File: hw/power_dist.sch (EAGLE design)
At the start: 72 parts, among them J1 JST-ZH6SMT_VERT, J2 JST-PH4SMT_VERT, J3 JST-PH5VERT, P1 XT30P, P2 XT30P, P3 XT30P, P4 XT30P, P5 XT30P, P6 XT30P, P7 XT90PW-M, Q1 PSMN4R8-100BSEJ, Q2 PSMN4R8-100BSEJ, Q3 PSMN4R8-100BSEJ, Q4 MF-DSC-SOT233-BSS138, Q5 MF-DSC-SOT233-MMBT3906, Q6 MF-DSC-SOT233-MMBT3904, U1 MAX15062AATA+T, U2 STM32G474CEU6, U3 LM5066IPMHE/NOPB, U4 TCAN334G

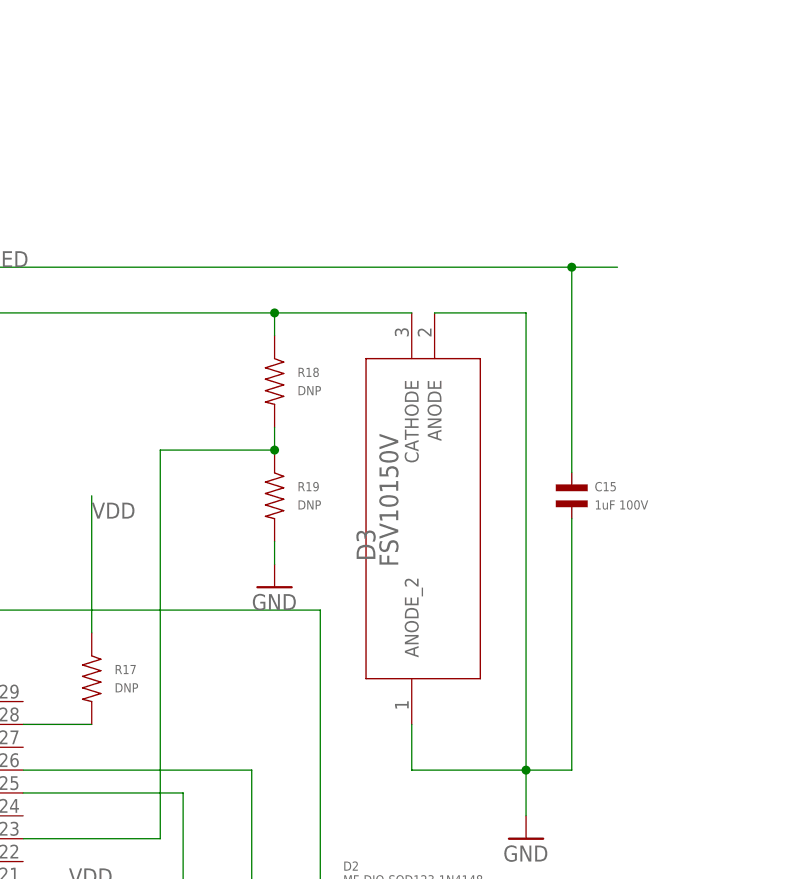
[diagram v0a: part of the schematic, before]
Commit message: Fix inconsistency in schematic
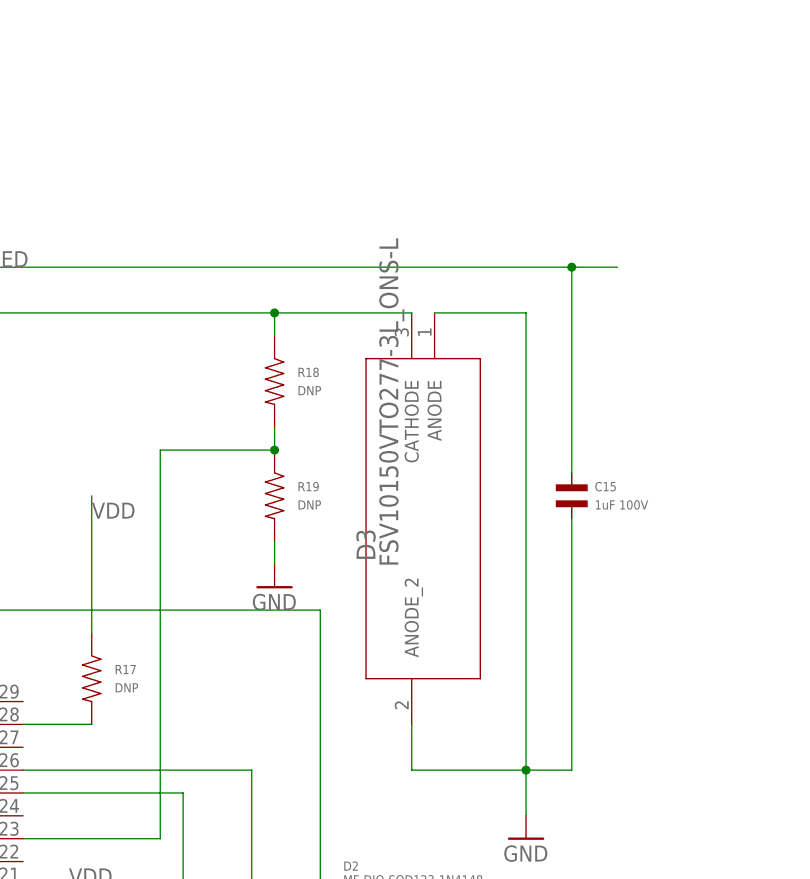
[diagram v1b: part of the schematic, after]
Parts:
- D3: value FSV10150V -> FSV10150VTO277-3L_ONS-L; device power_dist:FSV10150V -> power_dist:FSV10150VTO277-3L_ONS-L
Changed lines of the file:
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@@
 </part>
 <part name="GND7" library="supply1" deviceset="GND" device=""/>
-<part name="D3" library="power_dist" deviceset="FSV10150V" device="">
+<part name="D3" library="power_dist" deviceset="FSV10150V" device="TO277-3L_ONS-L" value="FSV10150VTO277-3L_ONS-L">
 <attribute name="MPN" value="FSV10150V"/>
 <attribute name="POPULATE" value="1"/>

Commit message: Draft r4.1 based on the LTC4380
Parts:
- removed Q6: MF-DSC-SOT233-MMBT3904, mfdiscretesemi:NPN_BJTMMBT3904_SOT-23-3
- removed R18, R19: DNP, mfpassives:RESISTOR_0603
- removed U3: LM5066IPMHE/NOPB, power_dist:LM5066IPMHE/NOPB
- added C18: 0.1uF, mfpassives:CAPACITOR_NP_0603
- added D6: MF-DIO-SOD123-1N4148, mfdiscretesemi:DIODES_1N4148_SOD-123
- added U$5: LTC4830, power_dist:LTC4830
- added U5: LT1787HVIMS8PBF, LT1787HVIMS8PBF:LT1787HVIMS8PBF
- C11: value 1uF -> (none); MPN MF-CAP-0603-1uF -> (none)
- C12: value 1uF -> DNP; HOUSEPART 1 -> (none); MPN MF-CAP-0603-1uF -> (none); POPULATE (none) -> 0
- C13: value 0.01uF -> 0.1uF; MPN MF-CAP-0603-0.01uF -> MF-CAP-0603-0.1uF
- C14: value 0.01uF -> 1uF 100V; device mfpassives:CAPACITOR_NP_0603 -> mfpassives:CAPACITOR_NP_0805; HOUSEPART 1 -> (none); MF (none) -> MURATA; MPN MF-CAP-0603-0.01uF -> GCM21BC72A105KE36L
- D2: HOUSEPART 1 -> (none)
- Q4: value MF-DSC-SOT233-BSS138 -> MF-DSC-SOT233-MMBT3904; device mfdiscretesemi:N-CHANNEL_FET_BSS138_SOT-23-3 -> mfdiscretesemi:NPN_BJTMMBT3904_SOT-23-3; HOUSEPART 1 -> (none)
- Q5: value MF-DSC-SOT233-MMBT3906 -> MMBT5401 100V; HOUSEPART 1 -> (none); MF (none) -> DIODES; MPN (none) -> MMBT5401-7-F
- R1, R2, R3: value 10k -> (none); MPN MF-RES-0603-10K -> (none)
- R10: value 0.3mOhm -> 0.5mOhm; MPN WSLF2512L3000FEA -> WSLF2512L5000FEA
- R11: value 24k 1% -> 200k 1%; HOUSEPART (none) -> 1; MF YAGEO -> (none); MPN RC0603FR-0724KL -> (none)
- R12: value 1k 1% -> 3M 1%; HOUSEPART (none) -> 1; MF YAGEO -> (none); MPN RC0603FR-071KL -> (none)
- R17: value DNP -> 200k 1%; HOUSEPART (none) -> 1; POPULATE 0 -> (none)
- R4: value 140k 1% -> 10k; HOUSEPART (none) -> 1; MF YAGEO -> (none); MPN RC0603FR-07140KL -> (none)
- R5: value 40.2k 1% -> 200k; HOUSEPART (none) -> 1; MF YAGEO -> (none); MPN RC0603FR-0740K2L -> (none)
- R6: value 100k 1% -> 1k; HOUSEPART (none) -> 1; MF YAGEO -> (none); MPN RC0603FR-07100KL -> (none)
- R7: value 40.2k 1% -> 2M; HOUSEPART (none) -> 1; MF YAGEO -> (none); MPN RC0603FR-0740K2L -> (none)
- R8: value 140k 1% -> 500k; HOUSEPART (none) -> 1; MF YAGEO -> (none); MPN RC0603FR-07140KL -> (none)
- R9: value 6.49k 1% -> 3M 1%; HOUSEPART (none) -> 1; MF YAGEO -> (none); MPN RC0603FR-076K49L -> (none)
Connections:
- removed net N$16: Q5.BASE, R12.P$2
- removed net N$3: Q6.BASE, Q6.COLLECTOR, U3.DIODE
- removed net PSHDN: Q4.GATE, R4.P$2, R5.P$1, U2.PB13
- removed net SCL: R2.P$1, U2.PA9, U3.SCL
- removed net SDA: R1.P$1, U2.PA8, U3.SDAI, U3.SDAO
- removed net SMBA: R3.P$1, U2.PA10, U3.!SMBA
- removed net VDD: C12.P$1, R17.P$1, U3.VDD
- removed net VIN_SENSE: R8.P$2, R9.P$1, U3.OVLO
- new net FLT: U$5.FLT, U2.PA5
- new net GATE: Q1.G, Q2.G, Q3.G, R1.P$2
- new net ISAMP: U2.PB10, U5.VOUT
- new net ISAMP_BIAS: C13.P$1, U2.PA4, U5.VBIAS
- new net LTC_EN: Q5.EMITTER, U$5.ON
- new net LTC_VCC: C14.P$1, R4.P$2, U$5.SEL, U$5.VCC
- new net N$17: D2.ANODE, R8.P$1
- new net N$18: D6.ANODE, R6.P$1
- new net PGND: C15.P$2, D3.ANODE, D3.ANODE_2, P1.1, P2.1, P3.1, P4.1, P5.1, P6.1, P7.1
- new net PWR_OVERRIDE: R6.P$2, U2.PA3
- new net SNS_PWR_SW: Q4.COLLECTOR, U2.PA2
- new net VIN_SAMP: R11.P$2, R9.P$1, U2.PB14
- new net VSWITCHED_SAMP: R12.P$1, R17.P$2, U2.PA7
- net +24V: now also J2.4, Q1.D, Q2.D, Q3.D, R3.P$2, R9.P$2; no longer R10.1, R6.P$1, R8.P$1, U3.VIN
- net GND: now also C18.P$2, J2.2, Q4.EMITTER, R11.P$1, R17.P$1, R5.P$1, U$5.GND, U5.VEE; no longer C12.P$2, C15.P$2, D3.ANODE, D3.ANODE_2, J2.4, P1.1, P2.1, P3.1, P4.1, P5.1, P6.1, P7.1, Q4.SOURCE, Q6.EMITTER, R11.P$2, R19.P$2, R5.P$2, R7.P$2, R9.P$2, U3.AGND, U3.GND
- net N$10: now also R3.P$1, U$5.DRN; no longer R11.P$1, U3.PWR
- net N$11: now also Q4.BASE, R7.P$1; no longer C13.P$1, U3.TIMER
- net N$12: now also C18.P$1, U$5.TMR; no longer R17.P$2, U3.PGD
- net N$13: now also D6.CATHODE, Q5.BASE, R5.P$2; no longer C14.P$1, Q5.EMITTER
- net N$5: now also R1.P$1, R2.P$2, U$5.GATE; no longer D2.ANODE, Q1.G, Q2.G, Q3.G, R12.P$1, U3.GATE
- net N$6: now also C12.P$1, U5.FIL-; no longer R18.P$2, R19.P$1, U3.FB
- net N$7: now also C12.P$2, U5.FIL+; no longer C11.P$1, U3.VREF
- net N$9: now also C11.P$1, R2.P$1; no longer Q4.DRAIN, R6.P$2, R7.P$1, U3.UVLO/EN
- net PWR_LED: now also R13.P$2, U2.PB12; no longer J2.2, U2.PB9
- net PWR_SW: now also R7.P$2, R8.P$2; no longer U2.PB7
- net VCC: no longer R1.P$2, R13.P$2, R2.P$2, R3.P$2
- net VIN_POST: now also Q1.S, Q2.S, Q3.S, R10.1; no longer Q1.D, Q2.D, Q3.D, R10.2
- net VSENSE_HIGH: now also U$5.SNS, U5.VS+; no longer U3.VIN_K
- net VSENSE_LOW: now also U$5.OUT, U5.VS-; no longer U3.SENSE
- net VSWITCHED: now also R10.2, R12.P$2; no longer Q1.S, Q2.S, Q3.S, R18.P$1, U3.OUT
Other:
- note added: "mjbots power dist r4.1 (c) 2020 Josh Pieper, jjp@pobox.com Licensed under the Apache 2.0 License https://www.apache.org/licenses/LICENSE-2.0"
- note removed: "Min / Typ / Max Upper UVLO: 9.95 Lower UVLO: 8.82 Upper OVLO: 57.11 Lower OVLO: 54.87"
- note removed: "mjbots power dist r4.0 (c) 2020 Josh Pieper, jjp@pobox.com Licensed under the Apache 2.0 License https://www.apache.org/licenses/LICENSE-2.0"
- moved on the sheet: C11, C12, C13, C14, D2, DB_3, DB_G, DB_VIN, DB_VSW, Q5, R1, R10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

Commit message: Connect GND/PGND and fix XT90 TH size
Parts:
- added SH4: SHORTBIG, shorts:SHORTBIG
- U4: MF Analog -> TI; MPN LTC2875IS8 -> TCAN334GDR
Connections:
- net GND: now also SH4.P$1
- net PGND: now also SH4.P$2
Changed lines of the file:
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@@
 <part name="GND18" library="supply1" deviceset="GND" device=""/>
 <part name="U4" library="precharge" deviceset="TCAN334G" device="">
-<attribute name="MF" value="Analog"/>
-<attribute name="MPN" value="LTC2875IS8"/>
+<attribute name="MF" value="TI"/>
+<attribute name="MPN" value="TCAN334GDR"/>
 <attribute name="POPULATE" value="1"/>
 </part>
@@
 <part name="GND25" library="supply1" deviceset="GND" device=""/>
 <part name="P+6" library="supply1" library_urn="urn:adsk.eagle:library:371" deviceset="+24V" device=""/>
+<part name="SH4" library="shorts" deviceset="SHORT" device="BIG" value="SHORTBIG">
+<attribute name="POPULATE" value="0"/>
+</part>
 </parts>
 <sheets>
@@
 <attribute name="VALUE" x="439.42" y="154.94" size="1.778" layer="96" rot="R90"/>
 </instance>
-<instance part="GND22" gate="1" x="-7.62" y="111.76" smashed="yes">
-<attribute name="VALUE" x="-10.16" y="109.22" size="1.778" layer="96"/>
+<instance part="GND22" gate="1" x="-20.32" y="109.22" smashed="yes">
+<attribute name="VALUE" x="-22.86" y="106.68" size="1.778" layer="96"/>
 </instance>
 <instance part="U1" gate="A" x="172.72" y="132.08" smashed="yes">
@@
 <instance part="P+6" gate="1" x="233.68" y="-15.24" smashed="yes">
 <attribute name="VALUE" x="231.14" y="-20.32" size="1.778" layer="96" rot="R90"/>
+</instance>
+<instance part="SH4" gate="G$1" x="-10.16" y="111.76" smashed="yes">
+<attribute name="POPULATE" x="-10.16" y="111.76" size="1.778" layer="96" display="off"/>
+<attribute name="NAME" x="-12.3825" y="113.03" size="1.778" layer="95"/>
 </instance>
 </instances>
@@
 <wire x1="238.76" y1="-50.8" x2="238.76" y2="-53.34" width="0.1524" layer="91"/>
 <junction x="238.76" y="-50.8"/>
+</segment>
+<segment>
+<pinref part="GND22" gate="1" pin="GND"/>
+<pinref part="SH4" gate="G$1" pin="P$1"/>
+<wire x1="-20.32" y1="111.76" x2="-12.7" y2="111.76" width="0.1524" layer="91"/>
 </segment>
 </net>
@@
 <wire x1="-48.26" y1="139.7" x2="-30.48" y2="139.7" width="0.1524" layer="91"/>
 <wire x1="-30.48" y1="139.7" x2="-30.48" y2="121.92" width="0.1524" layer="91"/>
-<wire x1="-30.48" y1="121.92" x2="2.54" y2="121.92" width="0.1524" layer="91"/>
+<wire x1="-30.48" y1="121.92" x2="-5.08" y2="121.92" width="0.1524" layer="91"/>
 <pinref part="P1" gate="G$1" pin="1"/>
+<wire x1="-5.08" y1="121.92" x2="2.54" y2="121.92" width="0.1524" layer="91"/>
 <wire x1="2.54" y1="142.24" x2="10.16" y2="142.24" width="0.1524" layer="91"/>
 <pinref part="P2" gate="G$1" pin="1"/>
@@
 <wire x1="2.54" y1="121.92" x2="2.54" y2="142.24" width="0.1524" layer="91"/>
 <label x="5.08" y="121.92" size="1.778" layer="95"/>
-</segment>
-<segment>
+<pinref part="SH4" gate="G$1" pin="P$2"/>
+<wire x1="-7.62" y1="111.76" x2="-5.08" y2="111.76" width="0.1524" layer="91"/>
+<wire x1="-5.08" y1="111.76" x2="-5.08" y2="121.92" width="0.1524" layer="91"/>
+<junction x="-5.08" y="121.92"/>
+</segment>
+<segment>

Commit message: Resize and draft place all silks
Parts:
- added C19, C20: 0.01uF, mfpassives:CAPACITOR_NP_0603
- added D7, D8: MF-DIO-SOD123-1N4148, mfdiscretesemi:DIODES_1N4148_SOD-123
- added R18: DNP, mfpassives:RESISTOR_0603
- renumbered U$5 to U6
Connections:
- new net 3V3_EN: D7.CATHODE, D8.CATHODE, R18.P$2, U1.EN/UVLO
- new net 3V3_OVERRIDE: D8.ANODE, U2.PB13
- net +24V: no longer U1.EN/UVLO
- net GND: now also C19.P$2, C20.P$2, R18.P$1
- net VIN_POST: now also D7.ANODE
- net VIN_SAMP: now also C20.P$1
- net VSWITCHED_SAMP: now also C19.P$1

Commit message: Rename all resistors, capacitors, and diodes
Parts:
- removed D8: MF-DIO-SOD123-1N4148, mfdiscretesemi:DIODES_1N4148_SOD-123
- removed R16: DNP, mfpassives:RESISTOR_0603
- added !6: 500k, mfpassives:RESISTOR_0603
- added X3: FSV10150VTO277-3L_ONS-L, power_dist:FSV10150VTO277-3L_ONS-L
- C1: value 1uF 100V -> DNP; device mfpassives:CAPACITOR_NP_0805 -> mfpassives:CAPACITOR_NP_0603; MF MURATA -> (none); MPN GCM21BC72A105KE36L -> (none); POPULATE (none) -> 0
- C10, C4: value 0.1uF -> 10uF 50V; device mfpassives:CAPACITOR_NP_0603 -> mfpassives:CAPACITOR_NP_1206; HOUSEPART 1 -> (none); MF (none) -> TDK; MPN MF-CAP-0603-0.1uF -> C3216X7R1H106K160AE
- C11: value (none) -> 0.1uF; MPN (none) -> MF-CAP-0603-0.1uF
- C12: value DNP -> 1uF 100V; device mfpassives:CAPACITOR_NP_0603 -> mfpassives:CAPACITOR_NP_0805; MF (none) -> MURATA; MPN (none) -> GCM21BC72A105KE36L; POPULATE 0 -> (none)
- C13: value 0.1uF -> (none); MPN MF-CAP-0603-0.1uF -> (none)
- C14: value 1uF 100V -> 0.1uF; device mfpassives:CAPACITOR_NP_0805 -> mfpassives:CAPACITOR_NP_0603; HOUSEPART (none) -> 1; MF MURATA -> (none); MPN GCM21BC72A105KE36L -> MF-CAP-0603-0.1uF
- C16: value 0.1uF -> DNP; HOUSEPART 1 -> (none); MPN MF-CAP-0603-0.1uF -> (none); POPULATE (none) -> 0
- C17: value DNP -> 0.01uF; HOUSEPART (none) -> 1; MPN (none) -> MF-CAP-0603-0.01uF; POPULATE 0 -> (none)
- C18: value 0.1uF -> 0.01uF; MPN MF-CAP-0603-0.1uF -> MF-CAP-0603-0.01uF
- C19, C20: value 0.01uF -> 0.1uF; MPN MF-CAP-0603-0.01uF -> MF-CAP-0603-0.1uF
- C2: value 1uF -> 1uF 100V; device mfpassives:CAPACITOR_NP_0603 -> mfpassives:CAPACITOR_NP_0805; HOUSEPART 1 -> (none); MF (none) -> MURATA; MPN MF-CAP-0603-1uF -> GCM21BC72A105KE36L
- C3: value 10uF 50V -> 1uF; device mfpassives:CAPACITOR_NP_1206 -> mfpassives:CAPACITOR_NP_0603; HOUSEPART (none) -> 1; MF TDK -> (none); MPN C3216X7R1H106K160AE -> MF-CAP-0603-1uF
- C6: value 1uF -> 0.1uF; MPN MF-CAP-0603-1uF -> MF-CAP-0603-0.1uF
- C7: value 0.1uF -> 1uF; MPN MF-CAP-0603-0.1uF -> MF-CAP-0603-1uF
- C9: value 10uF 50V -> 0.1uF; device mfpassives:CAPACITOR_NP_1206 -> mfpassives:CAPACITOR_NP_0603; HOUSEPART (none) -> 1; MF TDK -> (none); MPN C3216X7R1H106K160AE -> MF-CAP-0603-0.1uF
- D1: value SMBJ51CA-E3/52 -> MF-DIO-SOD123-1N4148; device power_dist:SMBJ51CA-E3/52 -> mfdiscretesemi:DIODES_1N4148_SOD-123; MPN SMBJ51CA-E3/52 -> (none); POPULATE 1 -> (none)
- D3: value FSV10150VTO277-3L_ONS-L -> SMBJ51CA-E3/52; device power_dist:FSV10150VTO277-3L_ONS-L -> power_dist:SMBJ51CA-E3/52; MPN FSV10150V -> SMBJ51CA-E3/52
- R1: value (none) -> DNP; HOUSEPART 1 -> (none); POPULATE (none) -> 0
- R10: value 0.5mOhm -> 3M 1%; device power_dist:SENSE_RESISTOR2512 -> mfpassives:RESISTOR_0603; HOUSEPART (none) -> 1; MF VISHAY DALE -> (none); MPN WSLF2512L5000FEA -> (none); POPULATE 1 -> (none)
- R13: value 220 -> 200k 1%; MPN MF-RES-0603-220 -> (none)
- R15: value 220 -> 1k; MPN MF-RES-0603-220 -> (none)
- R17: value 200k 1% -> 2M
- R18: value DNP -> 200k
- R2: value (none) -> DNP
- R3: value (none) -> 10k
- R4: value 10k -> (none)
- R5: value 200k -> (none)
- R6: value 1k -> (none)
- R7: value 2M -> 0.5mOhm; device mfpassives:RESISTOR_0603 -> power_dist:SENSE_RESISTOR2512; HOUSEPART 1 -> (none); MF (none) -> VISHAY DALE; MPN (none) -> WSLF2512L5000FEA; POPULATE (none) -> 1
- R8: value 500k -> 220; MPN (none) -> MF-RES-0603-220
- R9: value 3M 1% -> 220; MPN (none) -> MF-RES-0603-220
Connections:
- net +24V: now also C2.P$1, D3.1, R10.P$2, R3.P$1, R4.P$2; no longer C1.P$1, D1.1, R3.P$2, R4.P$1, R9.P$2
- net 3V3_EN: now also D1.CATHODE, D2.CATHODE, R2.P$2; no longer D7.CATHODE, D8.CATHODE, R18.P$2
- net 3V3_OVERRIDE: now also D1.ANODE; no longer D8.ANODE
- net GATE: now also R5.P$2; no longer R1.P$2
- net GND: now also C12.P$2, D3.2, R1.P$2, R13.P$1, R2.P$1; no longer C16.P$2, D1.2, R16.P$2, R17.P$1, R5.P$1
- net ISAMP_BIAS: now also C19.P$1; no longer C13.P$1
- net LTC_VCC: now also C12.P$1, R3.P$2; no longer C14.P$1, R4.P$2
- net N$10: now also R4.P$1; no longer R3.P$1
- net N$11: now also R17.P$1; no longer R7.P$1
- net N$12: now also C14.P$1; no longer C18.P$1
- net N$13: now also D7.CATHODE, R18.P$2; no longer D2.CATHODE, R5.P$2
- net N$14: now also R9.P$1; no longer R15.P$1
- net N$15: now also C1.P$1, R1.P$1; no longer C17.P$1, R16.P$1
- net N$17: now also !6.P$1, D6.ANODE; no longer D2.ANODE, R8.P$1
- net N$18: now also D7.ANODE, R15.P$1; no longer D6.ANODE, R6.P$1
- net N$2: now also R14.P$1; no longer R13.P$1
- net N$4: now also C3.P$1; no longer C2.P$1
- net N$5: now also R5.P$1, R6.P$2; no longer R1.P$1, R2.P$2
- net N$6: now also C16.P$1; no longer C12.P$1
- net N$7: now also C16.P$2; no longer C12.P$2
- net N$8: now also R8.P$1; no longer R14.P$1
- net N$9: now also C13.P$1, R6.P$1; no longer C11.P$1, R2.P$1
- net NRST: now also C5.P$1; no longer C4.P$1
- net PGND: now also X3.ANODE, X3.ANODE_2; no longer D3.ANODE, D3.ANODE_2
- net PWR_LED: now also R14.P$2; no longer R13.P$2
- net PWR_OVERRIDE: now also R15.P$2; no longer R6.P$2
- net PWR_SW: now also !6.P$2, R17.P$2; no longer R7.P$2, R8.P$2
- net VCC: now also C11.P$1, C20.P$1, C4.P$1, R8.P$2, R9.P$2; no longer C16.P$1, C3.P$1, C5.P$1, R14.P$2, R15.P$2
- net VIN_POST: now also D2.ANODE, R7.1; no longer D7.ANODE, R10.1
- net VIN_SAMP: now also C17.P$1, R10.P$1; no longer C20.P$1, R9.P$1
- net VSENSE_HIGH: now also R7.S1; no longer R10.S1
- net VSENSE_LOW: now also R7.S2; no longer R10.S2
- net VSWITCHED: now also R7.2, X3.CATHODE; no longer D3.CATHODE, R10.2
- net VSWITCHED_SAMP: now also C18.P$1, R13.P$2; no longer C19.P$1, R17.P$2
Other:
- note added: "This circuit exists to keep the LTC disabled until the switch is closed, but also to draw minimal quiescent current both while it is disabled, and while the switch is closed and the LTC controller is enabled. Also, it supports the microcontroller latching the LTC on, while still being able to monitor the state of the actual power switch."
- moved on the sheet: C1, C10, C11, C12, C13, C14, C16, C17, C18, C19, C2, C20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

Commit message: Fine place silks
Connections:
- net GND: no longer D3.2
- net PGND: now also D3.2
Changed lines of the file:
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@@
 <attribute name="POPULATE" value="1"/>
 </part>
-<part name="GND7" library="supply1" deviceset="GND" device=""/>
 <part name="X3" library="power_dist" deviceset="FSV10150V" device="TO277-3L_ONS-L" value="FSV10150VTO277-3L_ONS-L">
 <attribute name="MPN" value="FSV10150V"/>
@@
 <attribute name="POPULATE" x="-63.5" y="7.62" size="1.778" layer="96" rot="R90" display="off"/>
 </instance>
-<instance part="GND7" gate="1" x="-63.5" y="-2.54" smashed="yes">
-<attribute name="VALUE" x="-66.04" y="-5.08" size="1.778" layer="96"/>
-</instance>
 <instance part="X3" gate="A" x="83.82" y="-25.4" smashed="yes" rot="R90">
 <attribute name="NAME" x="79.7814" y="-4.7244" size="2.0828" layer="95" ratio="6" rot="SR90"/>
@@
 <wire x1="154.94" y1="114.3" x2="165.1" y2="114.3" width="0.1524" layer="91"/>
 <junction x="165.1" y="114.3"/>
-</segment>
-<segment>
-<pinref part="D3" gate="A" pin="2"/>
-<pinref part="GND7" gate="1" pin="GND"/>
-<wire x1="-63.5" y1="7.62" x2="-63.5" y2="0" width="0.1524" layer="91"/>
 </segment>
 <segment>
@@
 <label x="96.52" y="-33.02" size="1.778" layer="95"/>
 </segment>
-</net>
+<segment>
+<pinref part="D3" gate="A" pin="2"/>
+<wire x1="-63.5" y1="7.62" x2="-63.5" y2="0" width="0.1524" layer="91"/>
+<label x="-66.04" y="-2.54" size="1.778" layer="95"/>
+</segment>
+</net>

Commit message: Fix a few minor glitches
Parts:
- renumbered !6 to R16
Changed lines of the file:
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@@
 <attribute name="HOUSEPART" value="1"/>
 </part>
-<part name="!6" library="mfpassives" deviceset="RESISTOR" device="_0603" value="500k">
+<part name="R16" library="mfpassives" deviceset="RESISTOR" device="_0603" value="500k">
 <attribute name="HOUSEPART" value="1"/>
 </part>
@@
 <attribute name="VALUE" x="496.316" y="-12.7" size="1.016" layer="96" font="vector" rot="R270"/>
 </instance>
-<instance part="!6" gate="G$1" x="480.06" y="-27.94" smashed="yes" rot="R270">
+<instance part="R16" gate="G$1" x="480.06" y="-27.94" smashed="yes" rot="R270">
 <attribute name="NAME" x="481.584" y="-30.48" size="1.016" layer="95" font="vector" rot="R270" align="top-left"/>
 <attribute name="VALUE" x="478.536" y="-30.48" size="1.016" layer="96" font="vector" rot="R270"/>
@@
 </segment>
 <segment>
-<pinref part="!6" gate="G$1" pin="P$2"/>
+<pinref part="R16" gate="G$1" pin="P$2"/>
 <label x="459.74" y="-27.94" size="1.778" layer="95"/>
 <wire x1="474.98" y1="-27.94" x2="459.74" y2="-27.94" width="0.1524" layer="91"/>
@@
 <net name="N$17" class="0">
 <segment>
-<pinref part="!6" gate="G$1" pin="P$1"/>
+<pinref part="R16" gate="G$1" pin="P$1"/>
 <pinref part="D6" gate="G$1" pin="ANODE"/>
 <wire x1="485.14" y1="-27.94" x2="487.68" y2="-27.94" width="0.1524" layer="91"/>
